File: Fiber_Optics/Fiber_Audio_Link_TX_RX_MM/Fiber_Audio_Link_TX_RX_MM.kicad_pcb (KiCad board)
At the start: 2 copper layers, 43 parts, among them J1 AudioJack4, J2 Conn_01x02, J3 Conn_01x10, J4 Conn_01x02, Q1 2N2222, Q2 Q_Photo_NPN, SW1 SW_SPDT, SW2 SW_SPDT, U1 LM358P, U2 LM386

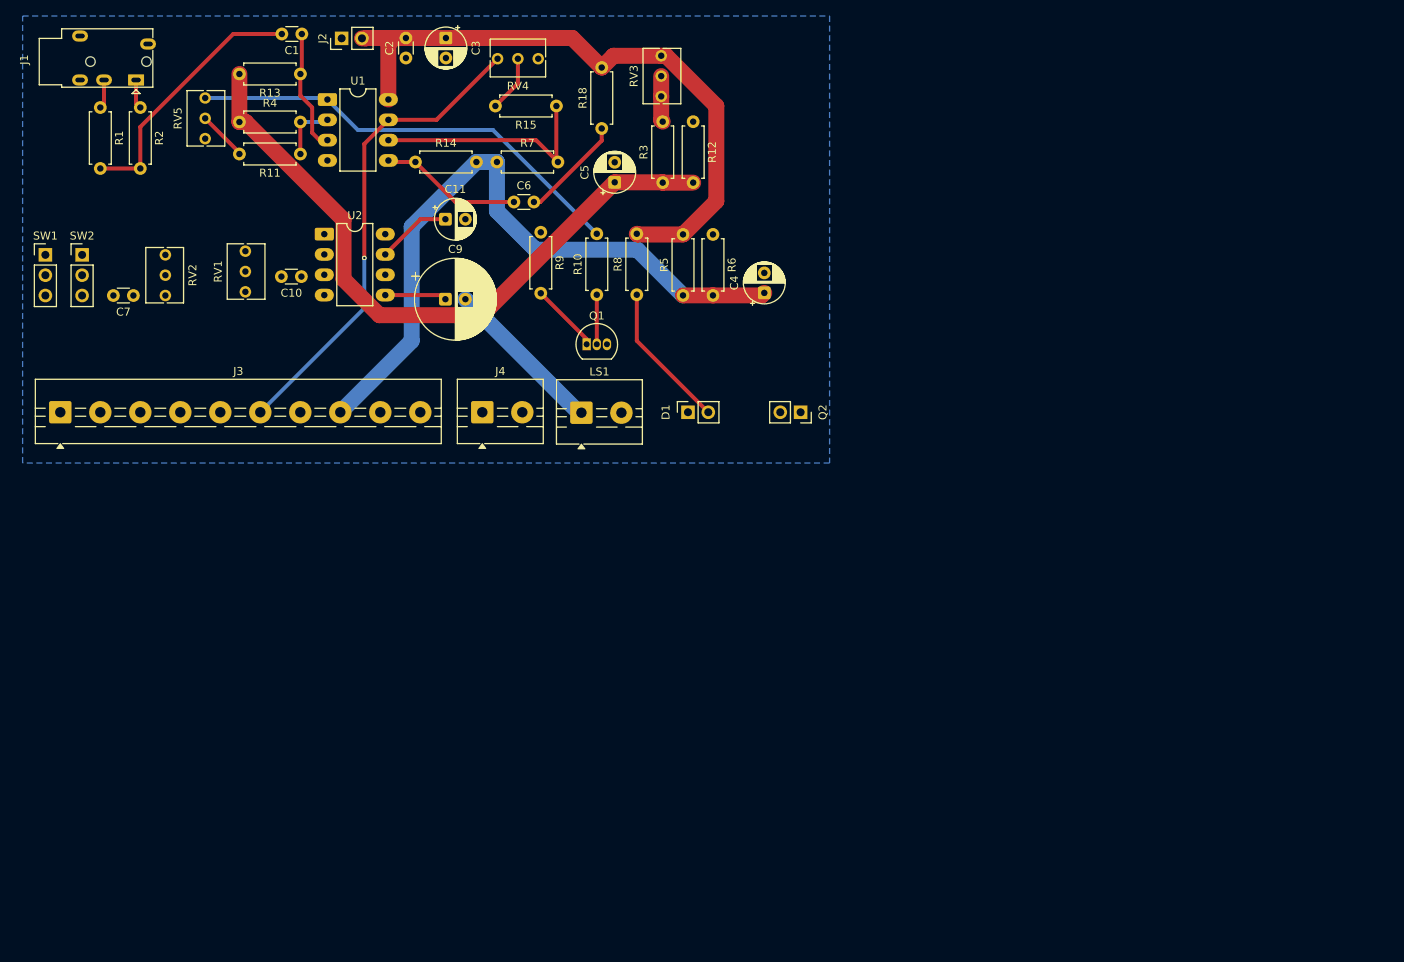
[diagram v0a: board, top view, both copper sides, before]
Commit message: update fiber audio link project.
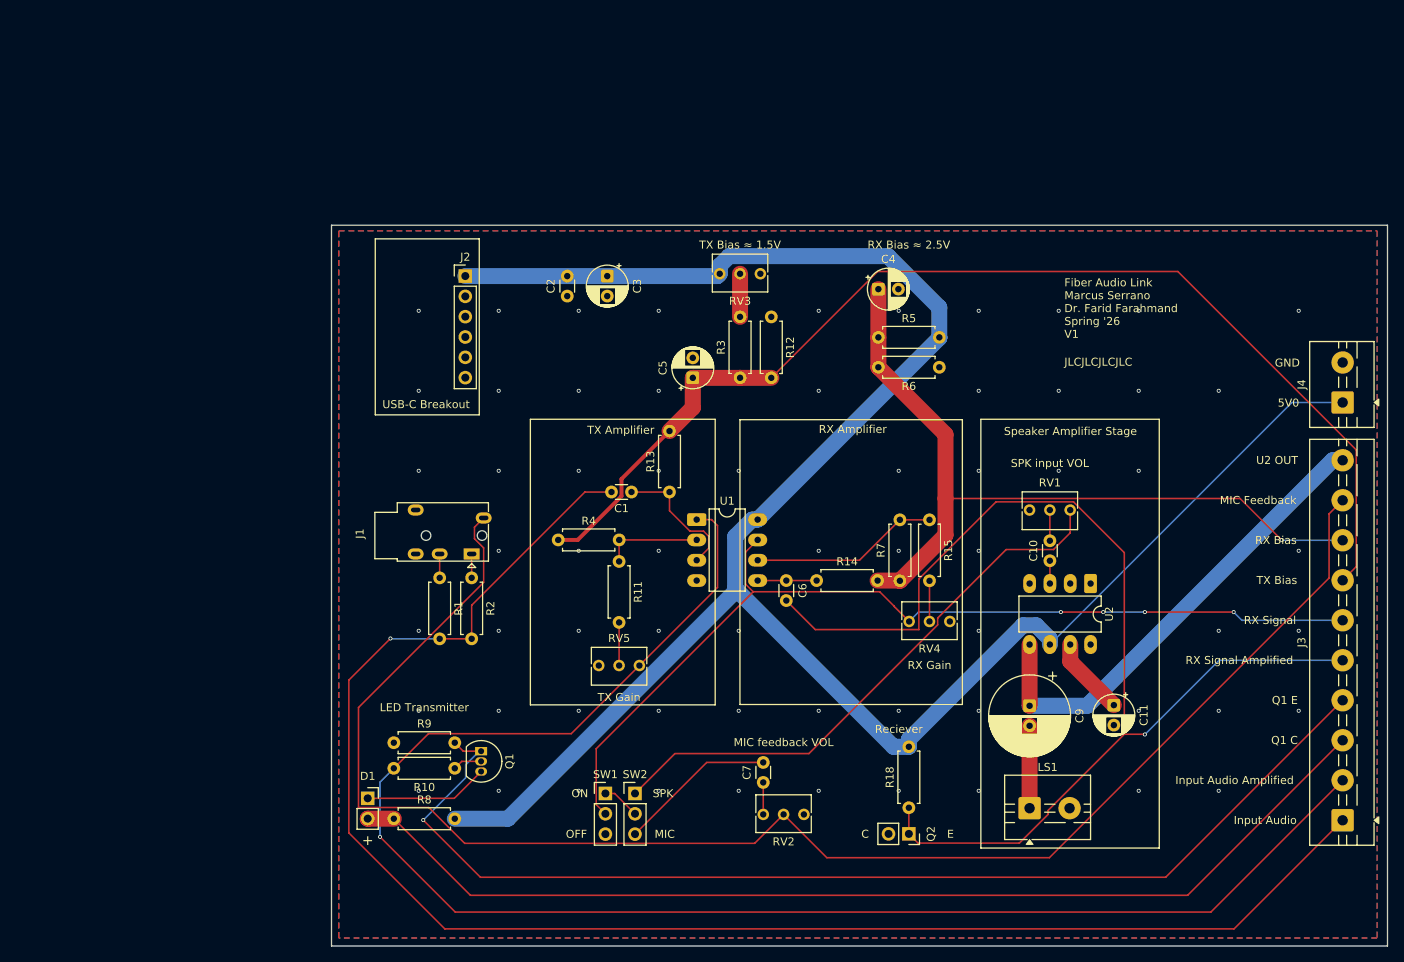
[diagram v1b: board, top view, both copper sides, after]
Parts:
- J2: value Conn_01x02 -> Conn_01x06; footprint Connector_PinHeader_2.54mm:PinHeader_1x02_P2.54mm_Vertical -> Connector_PinHeader_2.54mm:PinHeader_1x06_P2.54mm_Vertical
- moved J3 168.2 mm to (199.3, 132.3), turned to 90 degrees
- moved RV1 108.1 mm to (165.2, 93.5), turned to 0 degrees
- moved J4 107.6 mm to (199.3, 80.1), turned to 90 degrees
- moved U2 105.3 mm to (167.8, 102.7), turned to -90 degrees
- moved C11 103.3 mm to (170.7, 117.9), turned to -90 degrees
- moved C10 100.1 mm to (162.7, 99.8), turned to 90 degrees
- moved C7 99.5 mm to (126.9, 127.6), turned to 90 degrees
- moved RV2 99.0 mm to (126.9, 131.6), turned to 180 degrees
- moved SW1 97.1 mm to (107.1, 128.9)
- moved SW2 96.5 mm to (110.8, 128.9)
- moved R18 93.2 mm to (145.1, 130.7)
- moved RV5 89.3 mm to (111.4, 112.9), turned to 0 degrees
- moved C9 89.0 mm to (160.2, 118.0), turned to -90 degrees
- moved RV4 87.1 mm to (145.1, 107.4)
- moved LS1 74.7 mm to (160.2, 130.8)
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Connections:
- J2 pad 1: GND -> +5V
- J2 pad 2: +5V -> GND
- RV3 pad 3: Net-(R3-Pad2) -> unconnected-(RV3-Pad3)
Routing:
- net /Mic: track 0.00 -> 195.4 mm
- net +5V: track 82.1 -> 261.7 mm
- net /Mono: track 32.7 -> 199.0 mm, vias 0 -> 1
- net /Mono_Amplified: track 56.0 -> 200.8 mm, vias 0 -> 1
- net /Sig_RX: track 13.2 -> 147.2 mm, vias 0 -> 1
- net /Q1_E: track 8.75 -> 142.5 mm, vias 0 -> 1
- net /Q1_C: track 18.4 -> 133.9 mm
- net /Spk_In: track 0.00 -> 71.2 mm
- net /Sig_RX_Amplified: track 60.0 -> 120.0 mm, vias 1 -> 4
- net /V_Bias_TX: track 84.0 -> 143.3 mm
- net /U2_Out: track 7.73 -> 59.5 mm
- net /Mic_Out: track 0.00 -> 19.7 mm
- net Net-(D1-K): track 0.00 -> 15.6 mm
- net /V_Bias_RX: track 84.9 -> 96.9 mm, vias 0 -> 1
- net Net-(U1B-+): track 17.8 -> 7.37 mm
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- added copper zone on F.Cu, net GND
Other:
- board outline added: 132 x 90.1 mm
- board text added: "+"
- board text added: "5V0"
- board text added: "C"
- board text added: "E"
- board text added: "Fiber Audio Link Marcus Serrano Dr. Farid Farahmand Spring '26 V1"
- board text added: "GND"
- board text added: "Input Audio"
- board text added: "Input Audio Amplified"
- board text added: "JLCJLCJLCJLC"
- board text added: "LED Transmitter"
- board text added: "MIC"
- board text added: "MIC Feedback"
- board text added: "MIC feedback VOL"
- board text added: "OFF"
- board text added: "ON"
- board text added: "Q1 C"
- board text added: "Q1 E"
- board text added: "RX Amplifier"
- board text added: "RX Bias"
- board text added: "RX Bias ≈ 2.5V"
- board text added: "RX Gain"
- board text added: "RX Signal"
- board text added: "RX Signal Amplified"
- board text added: "Reciever"
- board text added: "SPK"
- board text added: "SPK input VOL"
- board text added: "Speaker Amplifier Stage"
- board text added: "TX Amplifier"
- board text added: "TX Bias"
- board text added: "TX Bias ≈ 1.5V"
- board text added: "TX Gain"
- board text added: "U2 OUT"
- board text added: "USB-C Breakout"
